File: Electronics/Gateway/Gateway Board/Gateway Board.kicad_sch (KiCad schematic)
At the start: 4 parts

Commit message: PCB Schematics finished
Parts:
- renumbered H1 to H101, H2 to H102, H3 to H103, H4 to H104
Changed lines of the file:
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@@
   (symbol (lib_id "Mechanical:MountingHole_Pad") (at 57.15 119.38 0) (unit 1)
     (in_bom yes) (on_board yes) (dnp no) (fields_autoplaced)
-    (property "Reference" "H4" (at 59.69 117.475 0)
+    (property "Reference" "H104" (at 59.69 117.475 0)
       (effects (font (size 1.27 1.27)) (justify left))
     )
@@
       (project "Gateway Board"
         (path "/5318664d-e328-4e84-a383-7318275dc447"
+          (reference "H104") (unit 1)
+        )
+      )
+      (project "Power Board"
+        (path "/d8843e0a-fd8a-4193-ba57-f0164156e030"
           (reference "H4") (unit 1)
         )
       )
-      (project "Power Board"
-        (path "/d8843e0a-fd8a-4193-ba57-f0164156e030"
-          (reference "H4") (unit 1)
-        )
-      )
     )
   )
   (symbol (lib_id "power:GND") (at 57.15 124.46 0) (unit 1)
     (in_bom yes) (on_board yes) (dnp no) (fields_autoplaced)
-    (property "Reference" "#PWR04" (at 57.15 130.81 0)
+    (property "Reference" "#PWR0104" (at 57.15 130.81 0)
       (effects (font (size 1.27 1.27)) hide)
     )
@@
       (project "Gateway Board"
         (path "/5318664d-e328-4e84-a383-7318275dc447"
+          (reference "#PWR0104") (unit 1)
+        )
+      )
+      (project "Power Board"
+        (path "/d8843e0a-fd8a-4193-ba57-f0164156e030"
           (reference "#PWR04") (unit 1)
         )
       )
-      (project "Power Board"
-        (path "/d8843e0a-fd8a-4193-ba57-f0164156e030"
-          (reference "#PWR04") (unit 1)
-        )
-      )
     )
   )
   (symbol (lib_id "Mechanical:MountingHole_Pad") (at 33.02 119.38 0) (unit 1)
     (in_bom yes) (on_board yes) (dnp no) (fields_autoplaced)
-    (property "Reference" "H2" (at 35.56 117.475 0)
+    (property "Reference" "H102" (at 35.56 117.475 0)
       (effects (font (size 1.27 1.27)) (justify left))
     )
@@
       (project "Gateway Board"
         (path "/5318664d-e328-4e84-a383-7318275dc447"
+          (reference "H102") (unit 1)
+        )
+      )
+      (project "Power Board"
+        (path "/d8843e0a-fd8a-4193-ba57-f0164156e030"
           (reference "H2") (unit 1)
         )
       )
-      (project "Power Board"
-        (path "/d8843e0a-fd8a-4193-ba57-f0164156e030"
-          (reference "H2") (unit 1)
-        )
-      )
     )
   )
   (symbol (lib_id "power:GND") (at 57.15 106.68 0) (unit 1)
     (in_bom yes) (on_board yes) (dnp no) (fields_autoplaced)
-    (property "Reference" "#PWR03" (at 57.15 113.03 0)
+    (property "Reference" "#PWR0103" (at 57.15 113.03 0)
       (effects (font (size 1.27 1.27)) hide)
     )
@@
       (project "Gateway Board"
         (path "/5318664d-e328-4e84-a383-7318275dc447"
+          (reference "#PWR0103") (unit 1)
+        )
+      )
+      (project "Power Board"
+        (path "/d8843e0a-fd8a-4193-ba57-f0164156e030"
           (reference "#PWR03") (unit 1)
         )
       )
-      (project "Power Board"
-        (path "/d8843e0a-fd8a-4193-ba57-f0164156e030"
-          (reference "#PWR03") (unit 1)
-        )
-      )
     )
   )
   (symbol (lib_id "Mechanical:MountingHole_Pad") (at 57.15 101.6 0) (unit 1)
     (in_bom yes) (on_board yes) (dnp no) (fields_autoplaced)
-    (property "Reference" "H3" (at 59.69 99.695 0)
+    (property "Reference" "H103" (at 59.69 99.695 0)
       (effects (font (size 1.27 1.27)) (justify left))
     )
@@
       (project "Gateway Board"
         (path "/5318664d-e328-4e84-a383-7318275dc447"
+          (reference "H103") (unit 1)
+        )
+      )
+      (project "Power Board"
+        (path "/d8843e0a-fd8a-4193-ba57-f0164156e030"
           (reference "H3") (unit 1)
         )
       )
-      (project "Power Board"
-        (path "/d8843e0a-fd8a-4193-ba57-f0164156e030"
-          (reference "H3") (unit 1)
-        )
-      )
     )
   )
   (symbol (lib_id "Mechanical:MountingHole_Pad") (at 33.02 101.6 0) (unit 1)
     (in_bom yes) (on_board yes) (dnp no) (fields_autoplaced)
-    (property "Reference" "H1" (at 35.56 99.695 0)
+    (property "Reference" "H101" (at 35.56 99.695 0)
       (effects (font (size 1.27 1.27)) (justify left))
     )
@@
       (project "Gateway Board"
         (path "/5318664d-e328-4e84-a383-7318275dc447"
+          (reference "H101") (unit 1)
+        )
+      )
+      (project "Power Board"
+        (path "/d8843e0a-fd8a-4193-ba57-f0164156e030"
           (reference "H1") (unit 1)
         )
       )
-      (project "Power Board"
-        (path "/d8843e0a-fd8a-4193-ba57-f0164156e030"
-          (reference "H1") (unit 1)
-        )
-      )
     )
   )
   (symbol (lib_id "power:GND") (at 33.02 106.68 0) (unit 1)
     (in_bom yes) (on_board yes) (dnp no) (fields_autoplaced)
-    (property "Reference" "#PWR01" (at 33.02 113.03 0)
+    (property "Reference" "#PWR0101" (at 33.02 113.03 0)
       (effects (font (size 1.27 1.27)) hide)
     )
@@
       (project "Gateway Board"
         (path "/5318664d-e328-4e84-a383-7318275dc447"
+          (reference "#PWR0101") (unit 1)
+        )
+      )
+      (project "Power Board"
+        (path "/d8843e0a-fd8a-4193-ba57-f0164156e030"
           (reference "#PWR01") (unit 1)
         )
       )
-      (project "Power Board"
-        (path "/d8843e0a-fd8a-4193-ba57-f0164156e030"
-          (reference "#PWR01") (unit 1)
-        )
-      )
     )
   )
   (symbol (lib_id "power:GND") (at 33.02 124.46 0) (unit 1)
     (in_bom yes) (on_board yes) (dnp no) (fields_autoplaced)
-    (property "Reference" "#PWR02" (at 33.02 130.81 0)
+    (property "Reference" "#PWR0102" (at 33.02 130.81 0)
       (effects (font (size 1.27 1.27)) hide)
     )
@@
       (project "Gateway Board"
         (path "/5318664d-e328-4e84-a383-7318275dc447"
-          (reference "#PWR02") (unit 1)
-        )
-      )
+          (reference "#PWR0102") (unit 1)
+        )
+      )

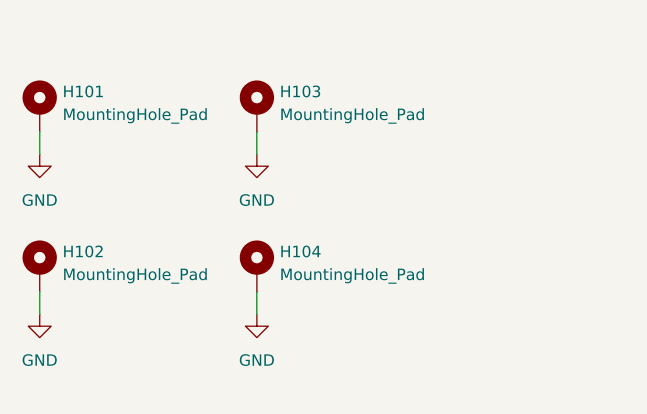
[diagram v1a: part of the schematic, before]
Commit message: Gateway board layout complete and routing begun
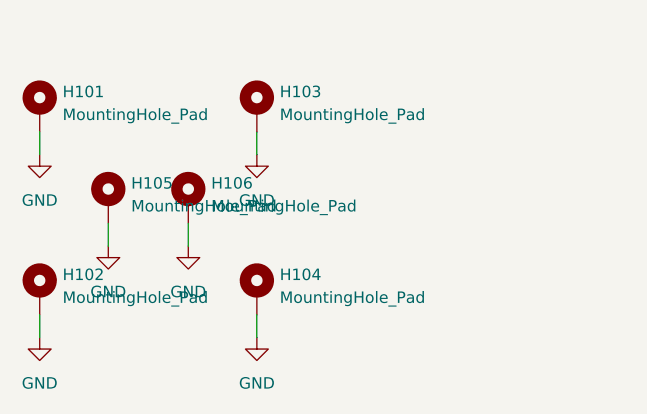
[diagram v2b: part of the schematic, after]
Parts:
- added H105, H106: MountingHole_Pad, MountingHole:MountingHole_3.2mm_M3_DIN965_Pad, symbol Mechanical:MountingHole_Pad
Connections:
- net GND: now also H105.1, H106.1
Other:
- moved on the sheet: H102, H104
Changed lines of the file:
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@@
 (kicad_sch (version 20230121) (generator eeschema)
   (paper "A5")
+  (wire (pts (xy 40.64 116.84) (xy 40.64 114.3))
+    (stroke (width 0) (type default))
+  )
   (wire (pts (xy 33.02 106.68) (xy 33.02 104.14))
     (stroke (width 0) (type default))
   )
+  (wire (pts (xy 49.53 116.84) (xy 49.53 114.3))
+    (stroke (width 0) (type default))
+  )
   (wire (pts (xy 57.15 106.68) (xy 57.15 104.14))
     (stroke (width 0) (type default))
   )
-  (wire (pts (xy 33.02 124.46) (xy 33.02 121.92))
-    (stroke (width 0) (type default))
-  )
-  (wire (pts (xy 57.15 124.46) (xy 57.15 121.92))
-    (stroke (width 0) (type default))
-  )
-  (symbol (lib_id "Mechanical:MountingHole_Pad") (at 57.15 119.38 0) (unit 1)
-    (in_bom yes) (on_board yes) (dnp no) (fields_autoplaced)
-    (property "Reference" "H104" (at 59.69 117.475 0)
-      (effects (font (size 1.27 1.27)) (justify left))
-    )
-    (property "Value" "MountingHole_Pad" (at 59.69 120.015 0)
-      (effects (font (size 1.27 1.27)) (justify left))
-    )
-    (property "Footprint" "MountingHole:MountingHole_3.2mm_M3_DIN965_Pad" (at 57.15 119.38 0)
-      (effects (font (size 1.27 1.27)) hide)
-    )
-    (property "Datasheet" "~" (at 57.15 119.38 0)
+  (wire (pts (xy 33.02 127) (xy 33.02 124.46))
+    (stroke (width 0) (type default))
+  )
+  (wire (pts (xy 57.15 127) (xy 57.15 124.46))
+    (stroke (width 0) (type default))
+  )
+  (symbol (lib_id "Mechanical:MountingHole_Pad") (at 57.15 121.92 0) (unit 1)
+    (in_bom yes) (on_board yes) (dnp no) (fields_autoplaced)
+    (property "Reference" "H104" (at 59.69 120.015 0)
+      (effects (font (size 1.27 1.27)) (justify left))
+    )
+    (property "Value" "MountingHole_Pad" (at 59.69 122.555 0)
+      (effects (font (size 1.27 1.27)) (justify left))
+    )
+    (property "Footprint" "MountingHole:MountingHole_3.2mm_M3_DIN965_Pad" (at 57.15 121.92 0)
+      (effects (font (size 1.27 1.27)) hide)
+    )
+    (property "Datasheet" "~" (at 57.15 121.92 0)
       (effects (font (size 1.27 1.27)) hide)
     )
@@
     )
   )
-  (symbol (lib_id "power:GND") (at 57.15 124.46 0) (unit 1)
-    (in_bom yes) (on_board yes) (dnp no) (fields_autoplaced)
-    (property "Reference" "#PWR0104" (at 57.15 130.81 0)
-      (effects (font (size 1.27 1.27)) hide)
-    )
-    (property "Value" "GND" (at 57.15 129.54 0)
-      (effects (font (size 1.27 1.27)))
-    )
-    (property "Footprint" "" (at 57.15 124.46 0)
-      (effects (font (size 1.27 1.27)) hide)
-    )
-    (property "Datasheet" "" (at 57.15 124.46 0)
+  (symbol (lib_id "power:GND") (at 57.15 127 0) (unit 1)
+    (in_bom yes) (on_board yes) (dnp no) (fields_autoplaced)
+    (property "Reference" "#PWR0104" (at 57.15 133.35 0)
+      (effects (font (size 1.27 1.27)) hide)
+    )
+    (property "Value" "GND" (at 57.15 132.08 0)
+      (effects (font (size 1.27 1.27)))
+    )
+    (property "Footprint" "" (at 57.15 127 0)
+      (effects (font (size 1.27 1.27)) hide)
+    )
+    (property "Datasheet" "" (at 57.15 127 0)
       (effects (font (size 1.27 1.27)) hide)
     )
@@
     )
   )
-  (symbol (lib_id "Mechanical:MountingHole_Pad") (at 33.02 119.38 0) (unit 1)
-    (in_bom yes) (on_board yes) (dnp no) (fields_autoplaced)
-    (property "Reference" "H102" (at 35.56 117.475 0)
-      (effects (font (size 1.27 1.27)) (justify left))
-    )
-    (property "Value" "MountingHole_Pad" (at 35.56 120.015 0)
-      (effects (font (size 1.27 1.27)) (justify left))
-    )
-    (property "Footprint" "MountingHole:MountingHole_3.2mm_M3_DIN965_Pad" (at 33.02 119.38 0)
-      (effects (font (size 1.27 1.27)) hide)
-    )
-    (property "Datasheet" "~" (at 33.02 119.38 0)
+  (symbol (lib_id "Mechanical:MountingHole_Pad") (at 40.64 111.76 0) (unit 1)
+    (in_bom yes) (on_board yes) (dnp no) (fields_autoplaced)
+    (property "Reference" "H105" (at 43.18 109.855 0)
+      (effects (font (size 1.27 1.27)) (justify left))
+    )
+    (property "Value" "MountingHole_Pad" (at 43.18 112.395 0)
+      (effects (font (size 1.27 1.27)) (justify left))
+    )
+    (property "Footprint" "MountingHole:MountingHole_3.2mm_M3_DIN965_Pad" (at 40.64 111.76 0)
+      (effects (font (size 1.27 1.27)) hide)
+    )
+    (property "Datasheet" "~" (at 40.64 111.76 0)
+      (effects (font (size 1.27 1.27)) hide)
+    )
+    (pin "1")
+    (instances
+      (project "Gateway Board"
+        (path "/5318664d-e328-4e84-a383-7318275dc447"
+          (reference "H105") (unit 1)
+        )
+      )
+      (project "Power Board"
+        (path "/d8843e0a-fd8a-4193-ba57-f0164156e030"
+          (reference "H2") (unit 1)
+        )
+      )
+    )
+  )
+  (symbol (lib_id "Mechanical:MountingHole_Pad") (at 33.02 121.92 0) (unit 1)
+    (in_bom yes) (on_board yes) (dnp no) (fields_autoplaced)
+    (property "Reference" "H102" (at 35.56 120.015 0)
+      (effects (font (size 1.27 1.27)) (justify left))
+    )
+    (property "Value" "MountingHole_Pad" (at 35.56 122.555 0)
+      (effects (font (size 1.27 1.27)) (justify left))
+    )
+    (property "Footprint" "MountingHole:MountingHole_3.2mm_M3_DIN965_Pad" (at 33.02 121.92 0)
+      (effects (font (size 1.27 1.27)) hide)
+    )
+    (property "Datasheet" "~" (at 33.02 121.92 0)
       (effects (font (size 1.27 1.27)) hide)
     )
@@
     )
   )
+  (symbol (lib_id "power:GND") (at 40.64 116.84 0) (unit 1)
+    (in_bom yes) (on_board yes) (dnp no) (fields_autoplaced)
+    (property "Reference" "#PWR0105" (at 40.64 123.19 0)
+      (effects (font (size 1.27 1.27)) hide)
+    )
+    (property "Value" "GND" (at 40.64 121.92 0)
+      (effects (font (size 1.27 1.27)))
+    )
+    (property "Footprint" "" (at 40.64 116.84 0)
+      (effects (font (size 1.27 1.27)) hide)
+    )
+    (property "Datasheet" "" (at 40.64 116.84 0)
+      (effects (font (size 1.27 1.27)) hide)
+    )
+    (pin "1")
+    (instances
+      (project "Gateway Board"
+        (path "/5318664d-e328-4e84-a383-7318275dc447"
+          (reference "#PWR0105") (unit 1)
+        )
+      )
+      (project "Power Board"
+        (path "/d8843e0a-fd8a-4193-ba57-f0164156e030"
+          (reference "#PWR02") (unit 1)
+        )
+      )
+    )
+  )
   (symbol (lib_id "Mechanical:MountingHole_Pad") (at 57.15 101.6 0) (unit 1)
     (in_bom yes) (on_board yes) (dnp no) (fields_autoplaced)
@@
     )
   )
+  (symbol (lib_id "power:GND") (at 49.53 116.84 0) (unit 1)
+    (in_bom yes) (on_board yes) (dnp no) (fields_autoplaced)
+    (property "Reference" "#PWR0106" (at 49.53 123.19 0)
+      (effects (font (size 1.27 1.27)) hide)
+    )
+    (property "Value" "GND" (at 49.53 121.92 0)
+      (effects (font (size 1.27 1.27)))
+    )
+    (property "Footprint" "" (at 49.53 116.84 0)
+      (effects (font (size 1.27 1.27)) hide)
+    )
+    (property "Datasheet" "" (at 49.53 116.84 0)
+      (effects (font (size 1.27 1.27)) hide)
+    )
+    (pin "1")
+    (instances
+      (project "Gateway Board"
+        (path "/5318664d-e328-4e84-a383-7318275dc447"
+          (reference "#PWR0106") (unit 1)
+        )
+      )
+      (project "Power Board"
+        (path "/d8843e0a-fd8a-4193-ba57-f0164156e030"
+          (reference "#PWR02") (unit 1)
+        )
+      )
+    )
+  )
   (symbol (lib_id "Mechanical:MountingHole_Pad") (at 33.02 101.6 0) (unit 1)
     (in_bom yes) (on_board yes) (dnp no) (fields_autoplaced)
@@
     )
   )
+  (symbol (lib_id "Mechanical:MountingHole_Pad") (at 49.53 111.76 0) (unit 1)
+    (in_bom yes) (on_board yes) (dnp no) (fields_autoplaced)
+    (property "Reference" "H106" (at 52.07 109.855 0)
+      (effects (font (size 1.27 1.27)) (justify left))
+    )
+    (property "Value" "MountingHole_Pad" (at 52.07 112.395 0)
+      (effects (font (size 1.27 1.27)) (justify left))
+    )
+    (property "Footprint" "MountingHole:MountingHole_3.2mm_M3_DIN965_Pad" (at 49.53 111.76 0)
+      (effects (font (size 1.27 1.27)) hide)
+    )
+    (property "Datasheet" "~" (at 49.53 111.76 0)
+      (effects (font (size 1.27 1.27)) hide)
+    )
+    (pin "1")
+    (instances
+      (project "Gateway Board"
+        (path "/5318664d-e328-4e84-a383-7318275dc447"
+          (reference "H106") (unit 1)
+        )
+      )
+      (project "Power Board"
+        (path "/d8843e0a-fd8a-4193-ba57-f0164156e030"
+          (reference "H3") (unit 1)
+        )
+      )
+    )
+  )
   (symbol (lib_id "power:GND") (at 33.02 106.68 0) (unit 1)
     (in_bom yes) (on_board yes) (dnp no) (fields_autoplaced)
@@
     )
   )
-  (symbol (lib_id "power:GND") (at 33.02 124.46 0) (unit 1)
-    (in_bom yes) (on_board yes) (dnp no) (fields_autoplaced)
-    (property "Reference" "#PWR0102" (at 33.02 130.81 0)
-      (effects (font (size 1.27 1.27)) hide)
-    )
-    (property "Value" "GND" (at 33.02 129.54 0)
-      (effects (font (size 1.27 1.27)))
-    )
-    (property "Footprint" "" (at 33.02 124.46 0)
-      (effects (font (size 1.27 1.27)) hide)
-    )
-    (property "Datasheet" "" (at 33.02 124.46 0)
-      (effects (font (size 1.27 1.27)) hide)
-    )
+  (symbol (lib_id "power:GND") (at 33.02 127 0) (unit 1)
+    (in_bom yes) (on_board yes) (dnp no) (fields_autoplaced)
+    (property "Reference" "#PWR0102" (at 33.02 133.35 0)
+      (effects (font (size 1.27 1.27)) hide)
+    )
+    (property "Value" "GND" (at 33.02 132.08 0)
+      (effects (font (size 1.27 1.27)))
+    )
+    (property "Footprint" "" (at 33.02 127 0)
+      (effects (font (size 1.27 1.27)) hide)
+    )
+    (property "Datasheet" "" (at 33.02 127 0)
+      (effects (font (size 1.27 1.27)) hide)
+    )
